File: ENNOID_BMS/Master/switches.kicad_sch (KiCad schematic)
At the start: 19 parts, among them Q3 BSS138, Q4 BUK98150-55A, Q5 BUK98150-55A, Q6 BUK98150-55A, Q7 BUK98150-55A, Q8 BUK98150-55A, Q9 BSS138

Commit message: ENNOID BMS PCBs completed
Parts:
- Q3, Q9: footprint TO_SOT_Packages_SMD:SOT-23 -> Package_TO_SOT_SMD:SOT-23
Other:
- note added: "this prevents the AIRS from accidentally being opened, but the condition for this should be understood maybe it can be used for the AMS OK signal"
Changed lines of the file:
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@@
+		)
+	)
+	(text "this prevents the AIRS from accidentally being opened, but the condition for this should be understood\nmaybe it can be used for the AMS OK signal"
+		(exclude_from_sim no)
+		(at 31.496 174.498 0)
+		(effects
+			(font
+				(size 1.27 1.27)
+			)
 		)
 	)
@@
 			)
 		)
-		(property "Footprint" "TO_SOT_Packages_SMD:SOT-23"
+		(property "Footprint" "Package_TO_SOT_SMD:SOT-23"
 			(at 149.86 172.085 0)
 			(effects
@@
 			)
 		)
-		(property "Footprint" "TO_SOT_Packages_SMD:SOT-23"
+		(property "Footprint" "Package_TO_SOT_SMD:SOT-23"
 			(at 175.26 172.085 0)
 			(effects

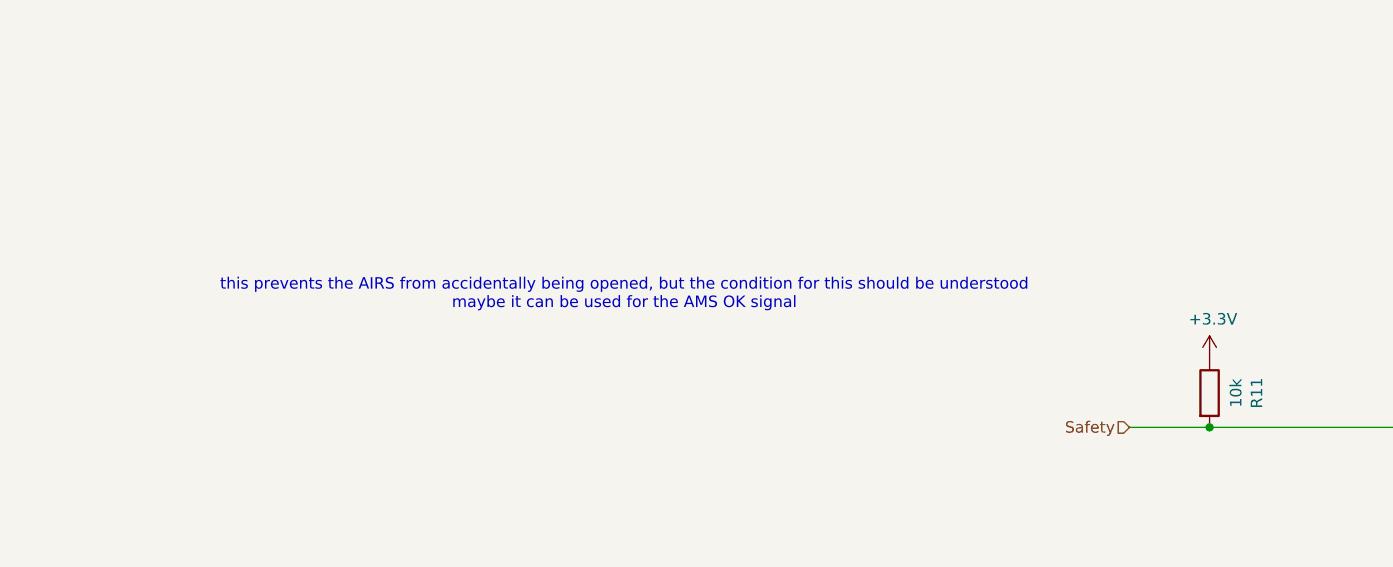
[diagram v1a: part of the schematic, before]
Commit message: slave with new fuses added
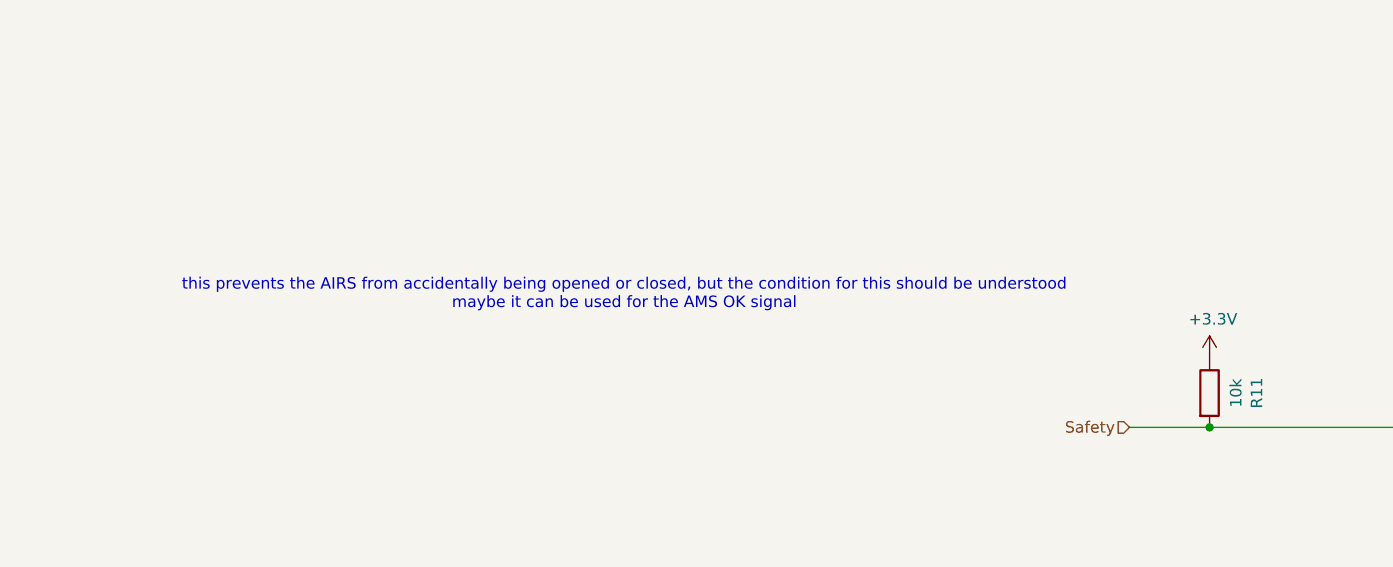
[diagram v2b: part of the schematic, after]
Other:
- note added: "this prevents the AIRS from accidentally being opened or closed, but the condition for this should be understood maybe it can be used for the AMS OK signal"
- note removed: "this prevents the AIRS from accidentally being opened, but the condition for this should be understood maybe it can be used for the AMS OK signal"
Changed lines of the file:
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@@
 		)
 	)
-	(text "this prevents the AIRS from accidentally being opened, but the condition for this should be understood\nmaybe it can be used for the AMS OK signal"
+	(text "this prevents the AIRS from accidentally being opened or closed, but the condition for this should be understood\nmaybe it can be used for the AMS OK signal"
 		(exclude_from_sim no)
 		(at 31.496 174.498 0)
